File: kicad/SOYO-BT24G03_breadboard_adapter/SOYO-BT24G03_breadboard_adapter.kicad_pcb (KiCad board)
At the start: 2 copper layers, 29.5 x 62.5 mm, 4 parts, among them J1 jack, P1 CONN_01X24, P2 CONN_01X23, U1 SOYO-BT24G03

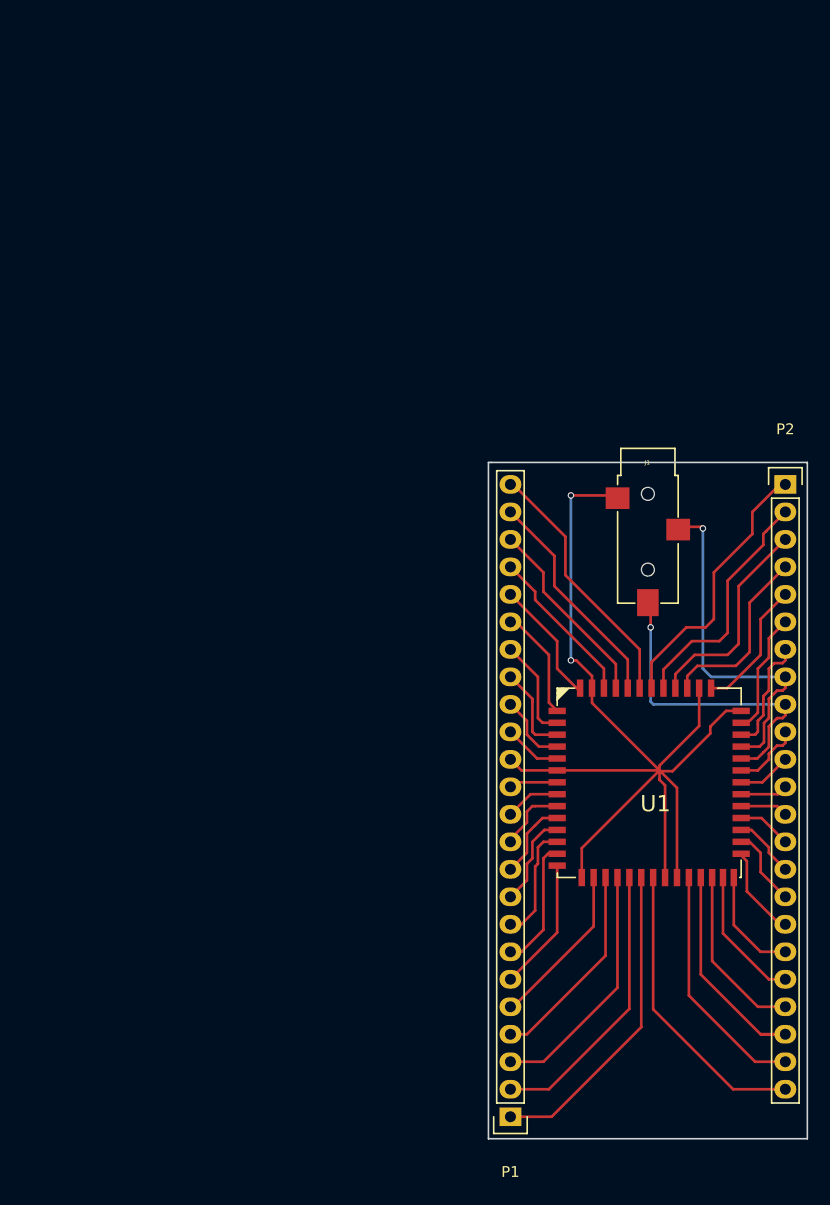
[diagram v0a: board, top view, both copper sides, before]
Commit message: revork board to be only 25.4mm wide, for fit inside bread board and leave space for cables on both sides
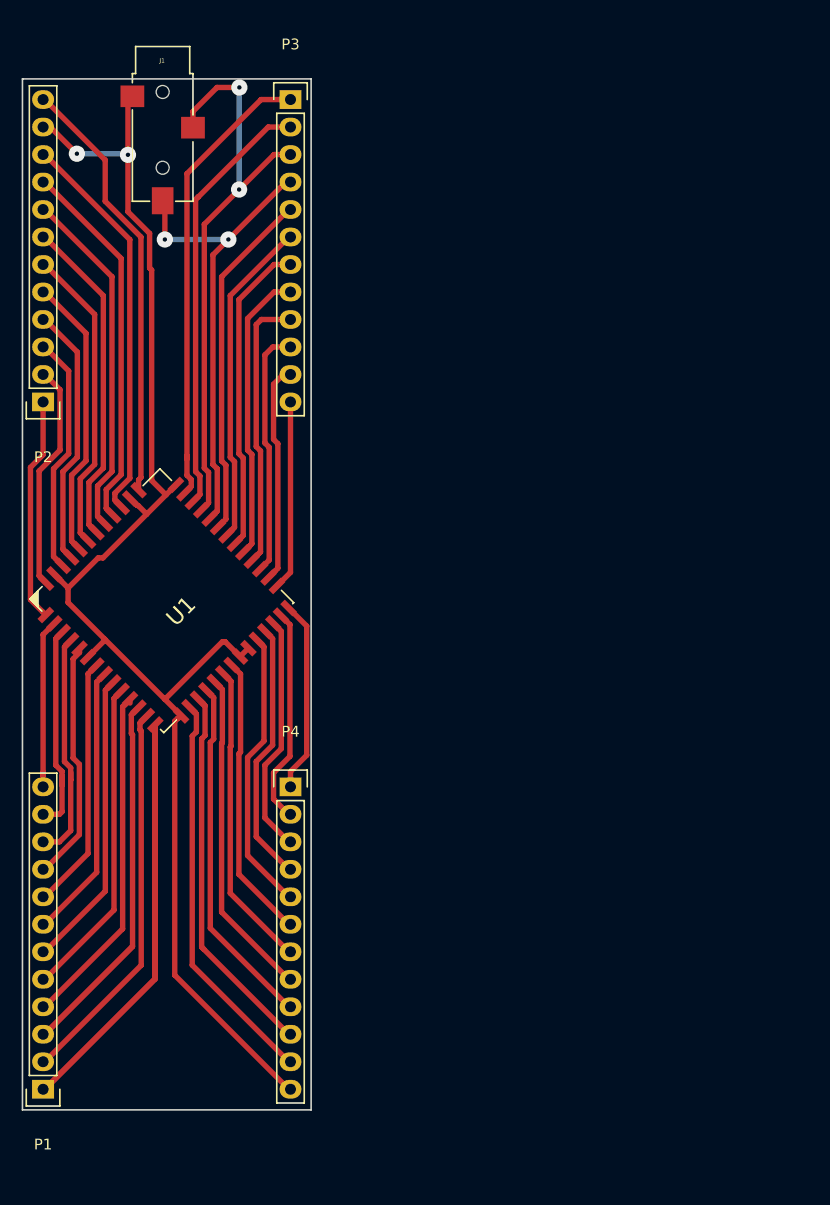
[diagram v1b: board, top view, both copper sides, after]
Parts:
- added P3: CONN_01X24, Pin_Headers:Pin_Header_Straight_1x12, F.Cu at (124.5, 33.0)
- added P4: CONN_01X24, Pin_Headers:Pin_Header_Straight_1x12, F.Cu at (124.5, 96.5)
- P1: footprint Pin_Headers:Pin_Header_Straight_1x24 -> Pin_Headers:Pin_Header_Straight_1x12
- P2: value CONN_01X23 -> CONN_01X24; footprint Pin_Headers:Pin_Header_Straight_1x23 -> Pin_Headers:Pin_Header_Straight_1x12
- moved P2 69.0 mm to (101.6, 61.0), turned to 180 degrees
- moved J1 58.2 mm to (112.6, 32.7)
- moved P1 43.3 mm to (101.6, 124.5)
- moved U1 38.7 mm to (112.7, 91.5), turned to 45 degrees
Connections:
- P2 pad 11: Net-(P2-Pad11) -> Net-(J1-Pad1)
- P2 pad 8: Net-(J1-Pad2) -> Net-(P2-Pad8)
- P2 pad 9: Net-(J1-Pad5) -> Net-(P2-Pad9)
- U1 pad 1: Net-(P1-Pad19) -> Net-(P2-Pad1)
- U1 pad 10: Net-(P1-Pad10) -> Net-(P1-Pad5)
- U1 pad 11: Net-(P1-Pad9) -> Net-(P1-Pad4)
- U1 pad 12: Net-(P1-Pad8) -> Net-(P1-Pad3)
- U1 pad 13: Net-(P1-Pad7) -> Net-(P1-Pad2)
- U1 pad 15: Net-(P1-Pad5) -> Net-(P4-Pad11)
- U1 pad 16: Net-(P1-Pad4) -> Net-(P4-Pad10)
- U1 pad 17: Net-(P1-Pad3) -> Net-(P4-Pad9)
- U1 pad 18: Net-(P1-Pad2) -> Net-(P4-Pad8)
- U1 pad 19: Net-(P1-Pad1) -> Net-(P4-Pad7)
- U1 pad 2: Net-(P1-Pad18) -> Net-(P1-Pad12)
- U1 pad 20: Net-(P2-Pad23) -> Net-(P4-Pad6)
- U1 pad 23: Net-(P2-Pad22) -> Net-(P4-Pad5)
- U1 pad 24: Net-(P2-Pad21) -> Net-(P4-Pad4)
- U1 pad 25: Net-(P2-Pad20) -> Net-(P4-Pad3)
- U1 pad 26: Net-(P2-Pad17) -> Net-(P3-Pad12)
- U1 pad 27: Net-(P2-Pad16) -> Net-(P3-Pad11)
- U1 pad 28: Net-(P2-Pad15) -> Net-(P3-Pad10)
- U1 pad 29: Net-(P2-Pad14) -> Net-(P3-Pad9)
- U1 pad 3: Net-(P1-Pad17) -> Net-(P1-Pad11)
- U1 pad 30: Net-(P2-Pad13) -> Net-(P3-Pad8)
- U1 pad 31: Net-(P2-Pad12) -> Net-(P3-Pad7)
- U1 pad 32: Net-(P2-Pad11) -> Net-(P3-Pad6)
- U1 pad 33: Net-(P2-Pad10) -> Net-(P3-Pad5)
- U1 pad 36: Net-(P2-Pad7) -> Net-(P3-Pad2)
- U1 pad 37: Net-(P2-Pad6) -> Net-(P3-Pad1)
- U1 pad 39: Net-(P2-Pad5) -> Net-(P2-Pad12)
- U1 pad 4: Net-(P1-Pad16) -> Net-(P1-Pad10)
- U1 pad 41: Net-(P2-Pad4) -> Net-(P2-Pad10)
- U1 pad 42: Net-(P2-Pad3) -> Net-(P2-Pad9)
- U1 pad 43: Net-(P2-Pad2) -> Net-(P2-Pad8)
- U1 pad 44: Net-(P2-Pad1) -> Net-(P2-Pad7)
- U1 pad 45: Net-(P1-Pad24) -> Net-(P2-Pad6)
- U1 pad 46: Net-(P1-Pad23) -> Net-(P2-Pad5)
- U1 pad 47: Net-(P1-Pad22) -> Net-(P2-Pad4)
- U1 pad 48: Net-(P1-Pad21) -> Net-(P2-Pad3)
- U1 pad 5: Net-(P1-Pad15) -> Net-(P1-Pad9)
- U1 pad 50: Net-(P1-Pad20) -> Net-(P2-Pad2)
- U1 pad 51: Net-(P2-Pad19) -> Net-(P4-Pad2)
- U1 pad 52: Net-(P2-Pad18) -> Net-(P4-Pad1)
- U1 pad 53: Net-(P1-Pad6) -> Net-(P1-Pad1)
- U1 pad 7: Net-(P1-Pad13) -> Net-(P1-Pad8)
- U1 pad 8: Net-(P1-Pad12) -> Net-(P1-Pad7)
- U1 pad 9: Net-(P1-Pad11) -> Net-(P1-Pad6)
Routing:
- net Net-(P1-Pad1): track 29.3 -> 75.5 mm
- net Net-(P3-Pad1): track 0.00 -> 42.7 mm
- net Net-(P3-Pad2): track 0.00 -> 39.9 mm
- net Net-(P4-Pad11): track 0.00 -> 37.0 mm
- net Net-(P4-Pad10): track 0.00 -> 36.1 mm
- net Net-(P2-Pad12): track 4.36 -> 40.0 mm
- net Net-(P2-Pad9): track 0.00 -> 34.7 mm
- net Net-(J1-Pad1): track 100.8 -> 133.9 mm
- net Net-(P4-Pad9): track 0.00 -> 32.8 mm
- net Net-(P2-Pad8): track 0.00 -> 32.6 mm
- net Net-(P3-Pad5): track 0.00 -> 32.5 mm
- net Net-(P4-Pad8): track 0.00 -> 30.5 mm
- net Net-(P3-Pad6): track 0.00 -> 30.4 mm
- net Net-(P2-Pad10): track 6.45 -> 36.8 mm
- net Net-(P3-Pad7): track 0.00 -> 29.2 mm
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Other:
- board size 29.5 x 62.5 mm -> 26.7 x 95.2 mm
- net class Default: clearance 0.2 -> 0.3; trace_width 0.25 -> 0.5; via_dia 0.6 -> 1.5
- rule trace_clearance: 0.2 -> 0.3
- rule trace_min: 0.2 -> 0.5
- rule via_min_size: 0.4 -> 1

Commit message: update pcb,jack, layout
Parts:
- J1: footprint jacks:3.5mm_stereo_jack_PJ3026 -> jacks:PJ-327A
- moved J1 2.13 mm to (112.9, 30.6)
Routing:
- net Net-(J1-Pad1): track 133.9 -> 142.5 mm
- net Net-(J1-Pad5): track 44.3 -> 50.7 mm
- net Net-(P3-Pad1): track 42.7 -> 48.2 mm
- net Net-(J1-Pad2): track 53.8 -> 48.6 mm

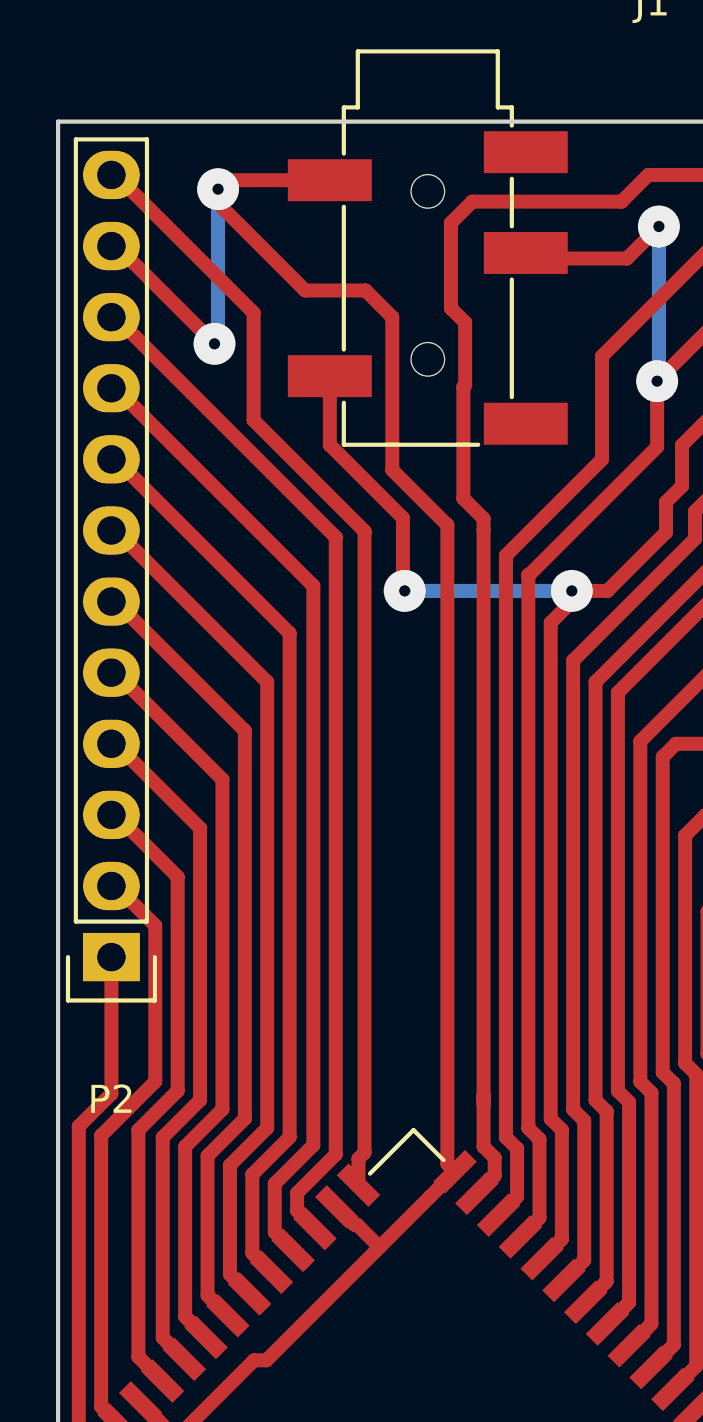
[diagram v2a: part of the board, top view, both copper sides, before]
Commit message: AGND pin separated from GND
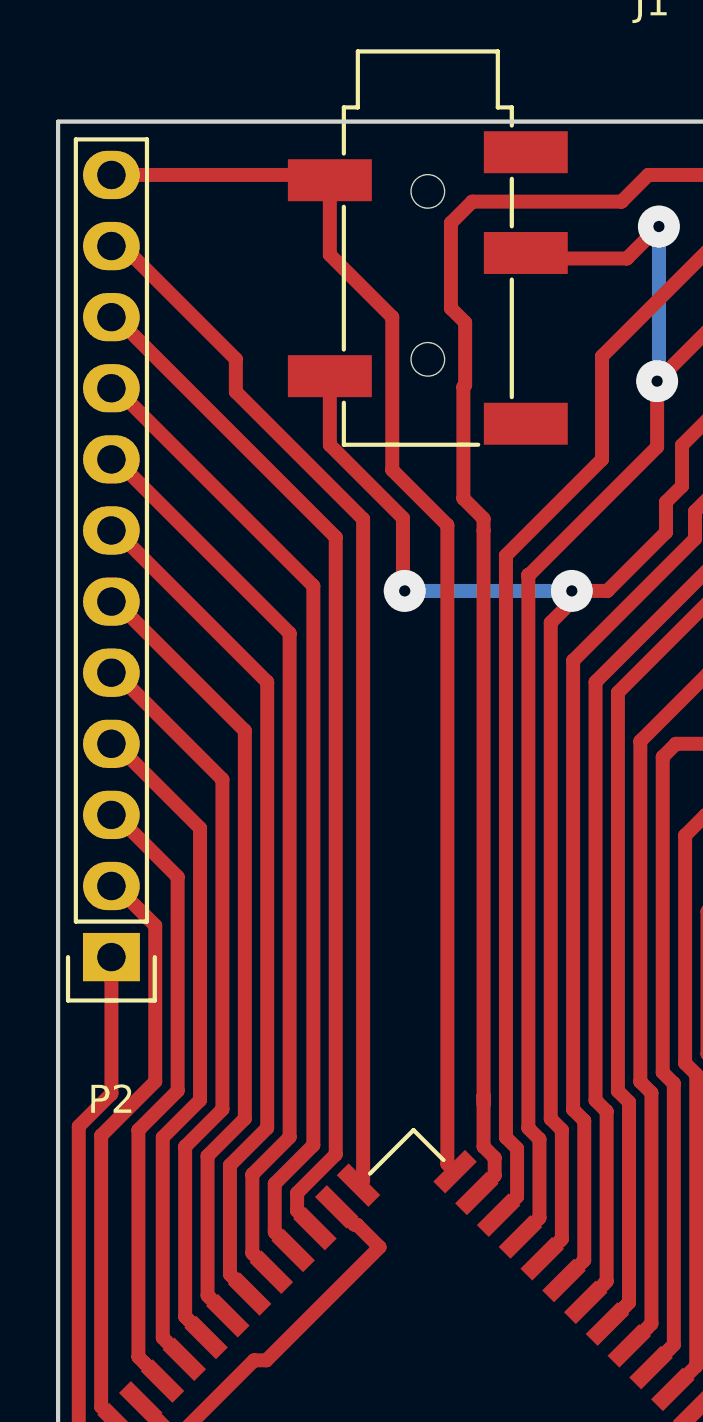
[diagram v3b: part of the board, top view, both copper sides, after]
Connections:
- P2 pad 11: Net-(J1-Pad1) -> Net-(P2-Pad11)
- P2 pad 12: Net-(P2-Pad12) -> Net-(J1-Pad1)
- P4 pad 12: Net-(J1-Pad1) -> Net-(P4-Pad12)
- U1 pad 14: Net-(J1-Pad1) -> Net-(P4-Pad12)
- U1 pad 21: Net-(J1-Pad1) -> Net-(P4-Pad12)
- U1 pad 22: Net-(J1-Pad1) -> Net-(P4-Pad12)
- U1 pad 39: Net-(P2-Pad12) -> Net-(P2-Pad11)
- U1 pad 40: Net-(J1-Pad1) -> Net-(P4-Pad12)
- U1 pad 49: Net-(J1-Pad1) -> Net-(P4-Pad12)
- U1 pad 6: Net-(J1-Pad1) -> Net-(P4-Pad12)
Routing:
- net Net-(J1-Pad1): track 142.5 -> 45.9 mm, vias 2 -> 0
- net Net-(P4-Pad12): track 0.00 -> 82.6 mm
- net Net-(P2-Pad12): track 40.0 -> 0.00 mm
- net Net-(P2-Pad11): track 0.00 -> 38.6 mm
